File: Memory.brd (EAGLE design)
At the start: 105.4 x 56.8 mm, 4 parts, among them IC5 HM62256DIP

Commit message: Finish Modularization
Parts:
- removed IC5: HM62256DIP, jean:HM62256-DIP
- added IC1: AT28C256ZIF, bt_memory:DIL28-ZIF
- added IC2: HM62256DIP, jean:HM62256-DIP
- U$1: value AT28C256ZIF -> (none); device bt_memory:DIL28-ZIF -> bfl:OSHW2
- moved U$1 31.4 mm to (43.2, 7.62), turned to 0 degrees
- moved V2 20.7 mm to (96.5, 21.6)
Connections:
- net !RD: now also IC1.22, IC2.22; no longer IC5.22, U$1.22
- net !WR: now also IC1.27, IC2.27; no longer IC5.27, U$1.27
- net A0: now also IC1.10, IC2.10; no longer IC5.10, U$1.10
- net A1: now also IC1.9, IC2.9; no longer IC5.9, U$1.9
- net A10: now also IC1.21, IC2.21; no longer IC5.21, U$1.21
- net A11: now also IC1.23, IC2.23; no longer IC5.23, U$1.23
- net A12: now also IC1.2, IC2.2; no longer IC5.2, U$1.2
- net A13: now also IC1.26, IC2.26; no longer IC5.26, U$1.26
- net A14: now also IC1.1, IC2.1; no longer IC5.1, U$1.1
- net A2: now also IC1.8, IC2.8; no longer IC5.8, U$1.8
- net A3: now also IC1.7, IC2.7; no longer IC5.7, U$1.7
- net A4: now also IC1.6, IC2.6; no longer IC5.6, U$1.6
- net A5: now also IC1.5, IC2.5; no longer IC5.5, U$1.5
- net A6: now also IC1.4, IC2.4; no longer IC5.4, U$1.4
- net A7: now also IC1.3, IC2.3; no longer IC5.3, U$1.3
- net A8: now also IC1.25, IC2.25; no longer IC5.25, U$1.25
- net A9: now also IC1.24, IC2.24; no longer IC5.24, U$1.24
- net D0: now also IC1.11, IC2.11; no longer IC5.11, U$1.11
- net D1: now also IC1.12, IC2.12; no longer IC5.12, U$1.12
- net D2: now also IC1.13, IC2.13; no longer IC5.13, U$1.13
- net D3: now also IC1.15, IC2.15; no longer IC5.15, U$1.15
- net D4: now also IC1.16, IC2.16; no longer IC5.16, U$1.16
- net D5: now also IC1.17, IC2.17; no longer IC5.17, U$1.17
- net D6: now also IC1.18, IC2.18; no longer IC5.18, U$1.18
- net D7: now also IC1.19, IC2.19; no longer IC5.19, U$1.19
- net GND: now also IC1.14, IC2.14; no longer IC5.14, U$1.14
- net N$2: now also IC1.20; no longer U$1.20
- net N$9: now also IC2.20; no longer IC5.20
- net VCC: now also IC1.28, IC2.28; no longer IC5.28, U$1.28
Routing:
- net N$2: track 0.00 -> 150.9 mm, vias 0 -> 3
- net GND: track 0.00 -> 110.4 mm, vias 0 -> 1
- net !MREQ: track 13.3 -> 116.1 mm, vias 0 -> 2
- net VCC: track 27.7 -> 121.8 mm
- net A11: track 23.2 -> 98.3 mm, vias 0 -> 1
- net A15: track 11.2 -> 82.3 mm
- net D6: track 177.5 -> 109.8 mm, vias 0 -> 1
- net D4: track 200.1 -> 136.3 mm, vias 0 -> 2
- net A10: track 28.0 -> 91.5 mm, vias 0 -> 1
- net D5: track 191.5 -> 129.9 mm, vias 0 -> 4
- net !RD: track 44.8 -> 85.9 mm
- net !WR: track 68.9 -> 35.1 mm
- net A7: track 73.4 -> 41.1 mm
- net A6: track 75.3 -> 46.6 mm
- net D3: track 208.0 -> 179.5 mm, vias 0 -> 1
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- added copper zone on layer 1, net GND
- added copper zone on layer 16, net GND
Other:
- board size 105.4 x 56.8 mm -> 101.6 x 37.8 mm
- board text added: "CPD-80 Memory V1"

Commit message: Update names and font
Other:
- board text added: "CPD-80 Memory v1"
- board text removed: "CPD-80 Memory V1"
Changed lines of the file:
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@@
 <wire x1="102.85" y1="37.77" x2="1.27" y2="37.77" width="0.254" layer="20"/>
 <wire x1="1.27" y1="37.77" x2="1.27" y2="0" width="0.254" layer="20"/>
-<text x="2.54" y="33.02" size="1.778" layer="21">CPD-80 Memory V1</text>
+<text x="2.54" y="33.02" size="1.778" layer="21" font="fixed">CPD-80 Memory v1</text>
 <rectangle x1="98.7933" y1="31.8135" x2="99.1235" y2="31.8389" layer="21"/>
 <rectangle x1="98.5901" y1="31.8389" x2="99.1997" y2="31.8643" layer="21"/>

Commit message: Change Memoryboard
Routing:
- net VCC: track 121.8 -> 134.5 mm, vias 0 -> 1
- net !RD: track 85.9 -> 87.8 mm
- net !MREQ: track 116.1 -> 117.5 mm
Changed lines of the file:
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@@
 <setting verticaltext="up"/>
 </settings>
-<grid distance="0.05" unitdist="inch" unit="inch" style="lines" multiple="1" display="no" altdistance="0.005" altunitdist="inch" altunit="inch"/>
+<grid distance="0.05" unitdist="inch" unit="inch" style="lines" multiple="1" display="no" altdistance="0.025" altunitdist="inch" altunit="inch"/>
 <layers>
 <layer number="1" name="Top" color="4" fill="1" visible="yes" active="yes"/>
@@
 <contactref element="JP1" pad="5"/>
 <wire x1="13.716" y1="35.306" x2="7.62" y2="29.21" width="0.254" layer="1"/>
-<wire x1="88.9" y1="35.306" x2="76.454" y2="35.306" width="0.254" layer="1"/>
 <wire x1="76.454" y1="35.306" x2="13.716" y2="35.306" width="0.254" layer="1"/>
 <wire x1="96.52" y1="27.686" x2="88.9" y2="35.306" width="0.254" layer="1"/>
@@
 <wire x1="76.454" y1="35.306" x2="76.454" y2="34.036" width="0.254" layer="1"/>
 <via x="78.232" y="32.258" extent="1-16" drill="0.6096"/>
+<wire x1="76.454" y1="35.306" x2="88.9" y2="35.306" width="0.254" layer="1"/>
 </signal>
 <signal name="D3">
@@
 <wire x1="38.1" y1="8.89" x2="38.1" y2="13.97" width="0.254" layer="1"/>
 <wire x1="35.56" y1="6.35" x2="38.1" y2="8.89" width="0.254" layer="1"/>
-<wire x1="94.996" y1="29.21" x2="100.33" y2="29.21" width="0.254" layer="16"/>
-<wire x1="90.932" y1="33.274" x2="94.996" y2="29.21" width="0.254" layer="16"/>
-<wire x1="77.978" y1="33.274" x2="90.932" y2="33.274" width="0.254" layer="16"/>
-<wire x1="76.2" y1="31.496" x2="77.978" y2="33.274" width="0.254" layer="16"/>
-<wire x1="76.2" y1="26.416" x2="76.2" y2="31.496" width="0.254" layer="16"/>
-<wire x1="81.28" y1="21.336" x2="76.2" y2="26.416" width="0.254" layer="16"/>
-<wire x1="81.28" y1="12.954" x2="81.28" y2="21.336" width="0.254" layer="16"/>
-<wire x1="80.518" y1="12.192" x2="81.28" y2="12.954" width="0.254" layer="16"/>
-<wire x1="66.802" y1="12.192" x2="80.518" y2="12.192" width="0.254" layer="16"/>
-<wire x1="66.04" y1="12.954" x2="66.802" y2="12.192" width="0.254" layer="16"/>
-<wire x1="66.04" y1="18.034" x2="66.04" y2="12.954" width="0.254" layer="16"/>
-<wire x1="55.88" y1="28.194" x2="66.04" y2="18.034" width="0.254" layer="16"/>
-<wire x1="55.88" y1="30.226" x2="55.88" y2="28.194" width="0.254" layer="16"/>
-<wire x1="55.118" y1="30.988" x2="55.88" y2="30.226" width="0.254" layer="16"/>
-<wire x1="53.848" y1="30.988" x2="55.118" y2="30.988" width="0.254" layer="16"/>
-<wire x1="52.07" y1="29.21" x2="53.848" y2="30.988" width="0.254" layer="16"/>
-<wire x1="41.656" y1="13.97" x2="38.1" y2="13.97" width="0.254" layer="16"/>
-<wire x1="55.88" y1="28.194" x2="41.656" y2="13.97" width="0.254" layer="16"/>
+<wire x1="26.162" y1="12.446" x2="26.162" y2="10.922" width="0.254" layer="1"/>
+<wire x1="26.924" y1="13.208" x2="26.162" y2="12.446" width="0.254" layer="1"/>
+<wire x1="26.924" y1="15.24" x2="26.924" y2="13.208" width="0.254" layer="1"/>
+<wire x1="29.464" y1="17.78" x2="26.924" y2="15.24" width="0.254" layer="1"/>
+<wire x1="34.29" y1="17.78" x2="29.464" y2="17.78" width="0.254" layer="1"/>
+<wire x1="38.1" y1="13.97" x2="34.29" y2="17.78" width="0.254" layer="1"/>
+<wire x1="94.869" y1="29.2608" x2="100.1268" y2="29.2608" width="0.254" layer="16"/>
+<wire x1="90.9828" y1="33.147" x2="94.869" y2="29.2608" width="0.254" layer="16"/>
+<wire x1="77.724" y1="33.147" x2="90.9828" y2="33.147" width="0.254" layer="16"/>
+<wire x1="76.3524" y1="31.7754" x2="77.724" y2="33.147" width="0.254" layer="16"/>
+<wire x1="76.3524" y1="26.289" x2="76.3524" y2="31.7754" width="0.254" layer="16"/>
+<wire x1="81.153" y1="21.4884" x2="76.3524" y2="26.289" width="0.254" layer="16"/>
+<wire x1="81.153" y1="12.8016" x2="81.153" y2="21.4884" width="0.254" layer="16"/>
+<wire x1="80.4672" y1="12.1158" x2="81.153" y2="12.8016" width="0.254" layer="16"/>
+<wire x1="66.9798" y1="12.1158" x2="80.4672" y2="12.1158" width="0.254" layer="16"/>
+<wire x1="65.8368" y1="13.2588" x2="66.9798" y2="12.1158" width="0.254" layer="16"/>
+<wire x1="65.8368" y1="15.7734" x2="65.8368" y2="13.2588" width="0.254" layer="16"/>
+<wire x1="60.8076" y1="20.8026" x2="65.8368" y2="15.7734" width="0.254" layer="16"/>
+<wire x1="46.863" y1="20.8026" x2="53.4924" y2="20.8026" width="0.254" layer="16"/>
+<wire x1="53.4924" y1="20.8026" x2="60.8076" y2="20.8026" width="0.254" layer="16"/>
+<wire x1="40.2336" y1="14.1732" x2="46.863" y2="20.8026" width="0.254" layer="16"/>
+<wire x1="38.1762" y1="14.1732" x2="40.2336" y2="14.1732" width="0.254" layer="16"/>
+<wire x1="100.1268" y1="29.2608" x2="100.33" y2="29.21" width="0.254" layer="16"/>
+<wire x1="38.1762" y1="14.1732" x2="38.1" y2="13.97" width="0.254" layer="16"/>
+<wire x1="52.1208" y1="28.1178" x2="52.1208" y2="29.0322" width="0.254" layer="1"/>
+<wire x1="53.4924" y1="26.7462" x2="52.1208" y2="28.1178" width="0.254" layer="1"/>
+<wire x1="53.4924" y1="20.8026" x2="53.4924" y2="26.7462" width="0.254" layer="16"/>
+<wire x1="52.1208" y1="29.0322" x2="52.07" y2="29.21" width="0.254" layer="1"/>
+<via x="53.4924" y="26.7462" extent="1-16" drill="0.6096"/>
 </signal>
 <signal name="GND">
@@
 <wire x1="76.2" y1="12.954" x2="80.01" y2="9.144" width="0.254" layer="1"/>
 <wire x1="76.2" y1="30.226" x2="76.2" y2="12.954" width="0.254" layer="1"/>
-<wire x1="76.962" y1="30.988" x2="76.2" y2="30.226" width="0.254" layer="1"/>
-<wire x1="90.932" y1="30.988" x2="76.962" y2="30.988" width="0.254" layer="1"/>
-<wire x1="92.71" y1="29.21" x2="90.932" y2="30.988" width="0.254" layer="1"/>
 <via x="36.83" y="2.794" extent="1-16" drill="0.6096"/>
 <via x="62.23" y="2.794" extent="1-16" drill="0.6096"/>
+<wire x1="92.71" y1="29.21" x2="92.71" y2="30.48" width="0.254" layer="1"/>
+<wire x1="92.71" y1="30.48" x2="91.44" y2="31.75" width="0.254" layer="1"/>
+<wire x1="91.44" y1="31.75" x2="82.55" y2="31.75" width="0.254" layer="1"/>
+<wire x1="82.55" y1="31.75" x2="81.915" y2="31.115" width="0.254" layer="1"/>
+<wire x1="81.915" y1="31.115" x2="77.089" y2="31.115" width="0.254" layer="1"/>
+<wire x1="77.089" y1="31.115" x2="76.2" y2="30.226" width="0.254" layer="1"/>
 </signal>
 <signal name="N$9">
@@
 <contactref element="IC1" pad="22"/>
 <contactref element="JP1" pad="55"/>
-<wire x1="28.702" y1="8.128" x2="22.86" y2="13.97" width="0.254" layer="16"/>
-<wire x1="31.242" y1="8.128" x2="28.702" y2="8.128" width="0.254" layer="16"/>
+<wire x1="31.242" y1="8.128" x2="29.21" y2="8.128" width="0.254" layer="16"/>
+<wire x1="29.21" y1="8.128" x2="28.702" y2="8.128" width="0.254" layer="16"/>
 <wire x1="33.02" y1="6.35" x2="31.242" y2="8.128" width="0.254" layer="16"/>
 <wire x1="62.992" y1="33.528" x2="67.31" y2="29.21" width="0.254" layer="1"/>
@@
 <wire x1="16.764" y1="20.066" x2="16.764" y2="30.48" width="0.254" layer="1"/>
 <wire x1="22.86" y1="13.97" x2="16.764" y2="20.066" width="0.254" layer="1"/>
+<wire x1="29.21" y1="8.89" x2="29.21" y2="8.128" width="0.254" layer="16"/>
+<wire x1="27.686" y1="10.414" x2="29.21" y2="8.89" width="0.254" layer="16"/>
+<wire x1="27.686" y1="10.668" x2="27.686" y2="10.414" width="0.254" layer="16"/>
+<wire x1="26.416" y1="11.938" x2="27.686" y2="10.668" width="0.254" layer="16"/>
+<wire x1="25.654" y1="11.938" x2="26.416" y2="11.938" width="0.254" layer="16"/>
+<wire x1="25.146" y1="11.43" x2="25.654" y2="11.938" width="0.254" layer="16"/>
+<wire x1="24.892" y1="11.43" x2="25.146" y2="11.43" width="0.254" layer="16"/>
+<wire x1="22.86" y1="13.462" x2="24.892" y2="11.43" width="0.254" layer="16"/>
+<wire x1="22.86" y1="13.97" x2="22.86" y2="13.462" width="0.254" layer="16"/>
 </signal>
 <signal name="N$2">

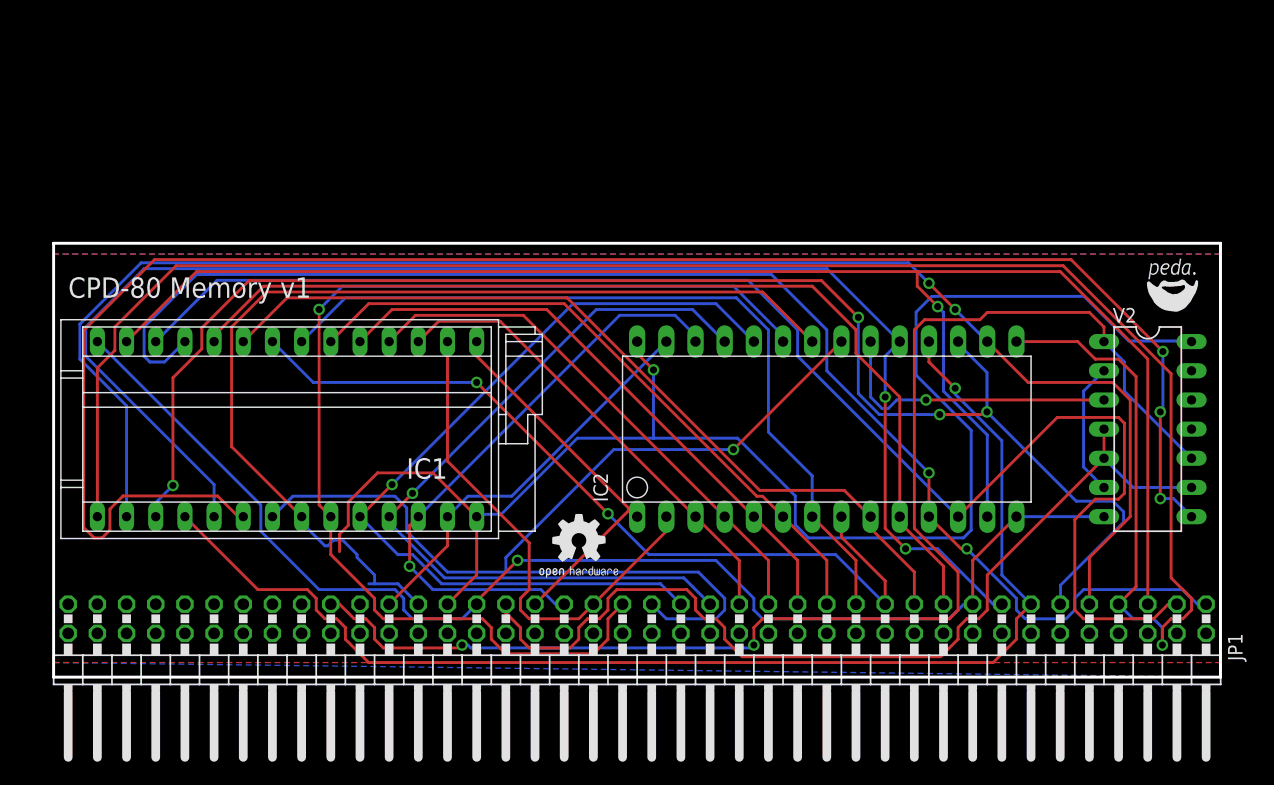
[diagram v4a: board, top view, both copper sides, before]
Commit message: Add Decoupling Capacitors.
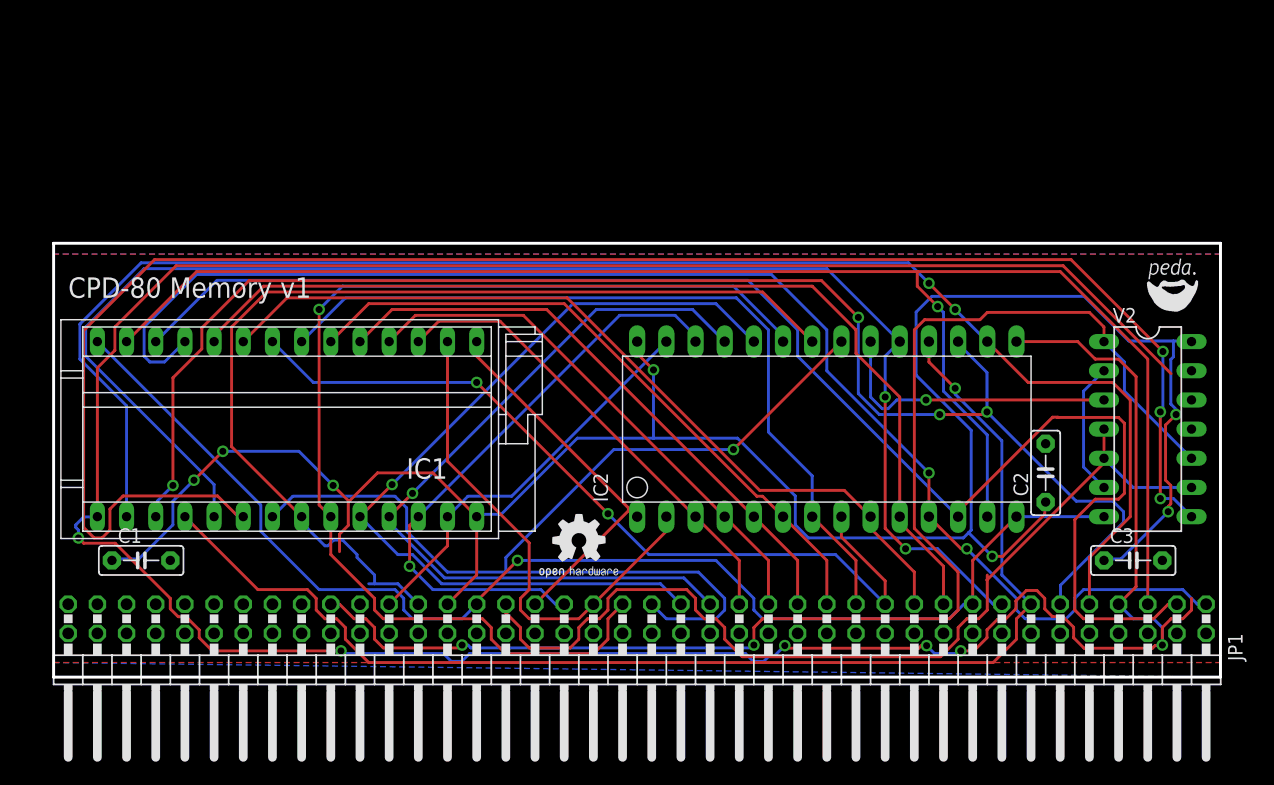
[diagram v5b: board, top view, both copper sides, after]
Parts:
- added C1, C2, C3: 0.1µF, capacitor-wima:C5B2.5
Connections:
- net GND: now also C1.2, C2.2, C3.2
- net VCC: now also C1.1, C2.1, C3.1
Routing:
- net D3: track 179.5 -> 270.3 mm, vias 1 -> 6
- net VCC: track 134.5 -> 195.4 mm, vias 1 -> 7

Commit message: Add Ground Rail to JEANNECTOR
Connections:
- net GND: now also JP1.10, JP1.12, JP1.14, JP1.16, JP1.18, JP1.2, JP1.20, JP1.22, JP1.24, JP1.26, JP1.28, JP1.30, JP1.32, JP1.34, JP1.36, JP1.38, JP1.4, JP1.40, JP1.42, JP1.44, JP1.46, JP1.48, JP1.50, JP1.52, JP1.54, JP1.56, JP1.58, JP1.6, JP1.60, JP1.62, JP1.64, JP1.66, JP1.68, JP1.70, JP1.72, JP1.74, JP1.76, JP1.78, JP1.8, JP1.80
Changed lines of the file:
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@@
 <contactref element="C2" pad="2"/>
 <contactref element="C3" pad="2"/>
-<wire x1="92.71" y1="13.97" x2="97.79" y2="10.16" width="0" layer="19" extent="1-1"/>
+<contactref element="JP1" pad="2"/>
+<contactref element="JP1" pad="4"/>
+<contactref element="JP1" pad="6"/>
+<contactref element="JP1" pad="8"/>
+<contactref element="JP1" pad="10"/>
+<contactref element="JP1" pad="12"/>
+<contactref element="JP1" pad="14"/>
+<contactref element="JP1" pad="16"/>
+<contactref element="JP1" pad="18"/>
+<contactref element="JP1" pad="20"/>
+<contactref element="JP1" pad="22"/>
+<contactref element="JP1" pad="24"/>
+<contactref element="JP1" pad="26"/>
+<contactref element="JP1" pad="28"/>
+<contactref element="JP1" pad="30"/>
+<contactref element="JP1" pad="32"/>
+<contactref element="JP1" pad="34"/>
+<contactref element="JP1" pad="36"/>
+<contactref element="JP1" pad="38"/>
+<contactref element="JP1" pad="40"/>
+<contactref element="JP1" pad="42"/>
+<contactref element="JP1" pad="44"/>
+<contactref element="JP1" pad="46"/>
+<contactref element="JP1" pad="48"/>
+<contactref element="JP1" pad="50"/>
+<contactref element="JP1" pad="52"/>
+<contactref element="JP1" pad="54"/>
+<contactref element="JP1" pad="56"/>
+<contactref element="JP1" pad="58"/>
+<contactref element="JP1" pad="60"/>
+<contactref element="JP1" pad="62"/>
+<contactref element="JP1" pad="64"/>
+<contactref element="JP1" pad="66"/>
+<contactref element="JP1" pad="68"/>
+<contactref element="JP1" pad="70"/>
+<contactref element="JP1" pad="72"/>
+<contactref element="JP1" pad="74"/>
+<contactref element="JP1" pad="76"/>
+<contactref element="JP1" pad="78"/>
+<contactref element="JP1" pad="80"/>
+<wire x1="97.79" y1="10.16" x2="92.71" y2="13.97" width="0" layer="19" extent="1-1"/>
 </signal>
 <signal name="!MREQ">

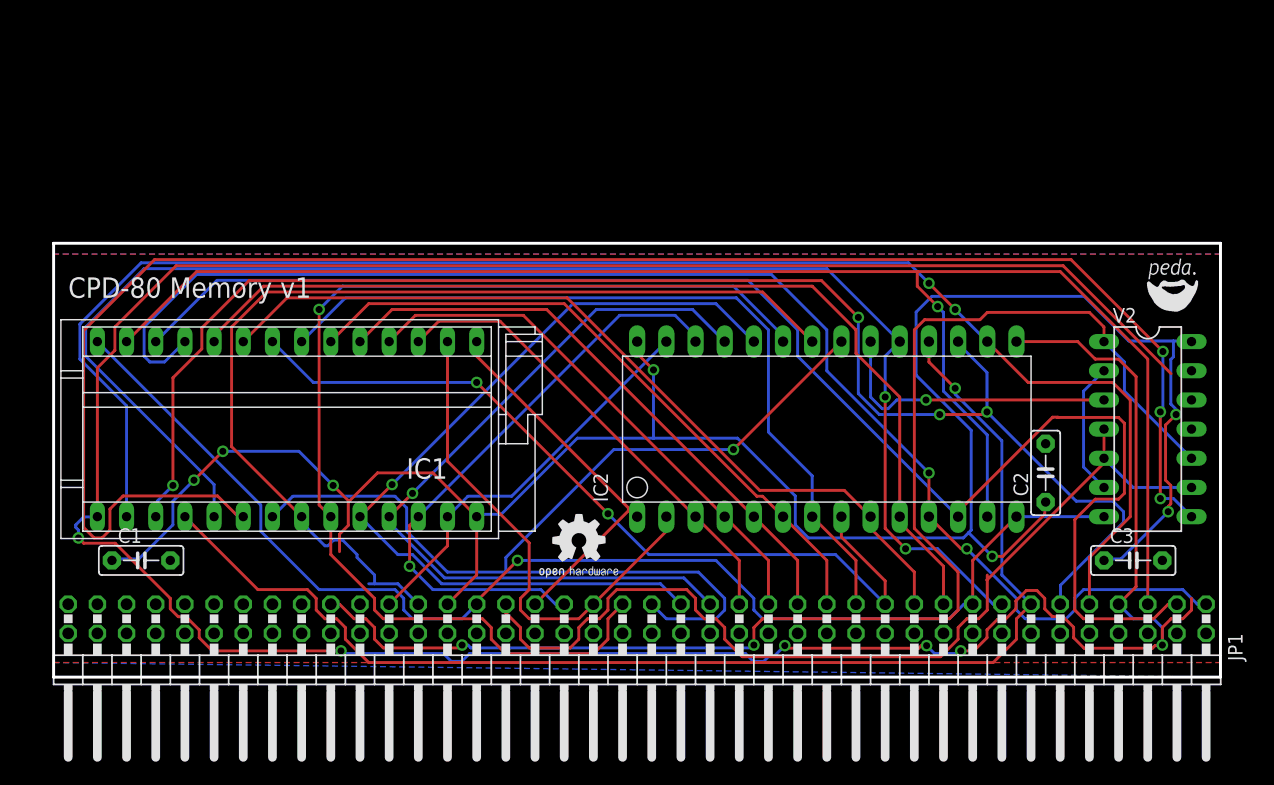
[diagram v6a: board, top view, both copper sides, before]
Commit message: Make Top Plane a VCC Plane instead of Ground, add Holes
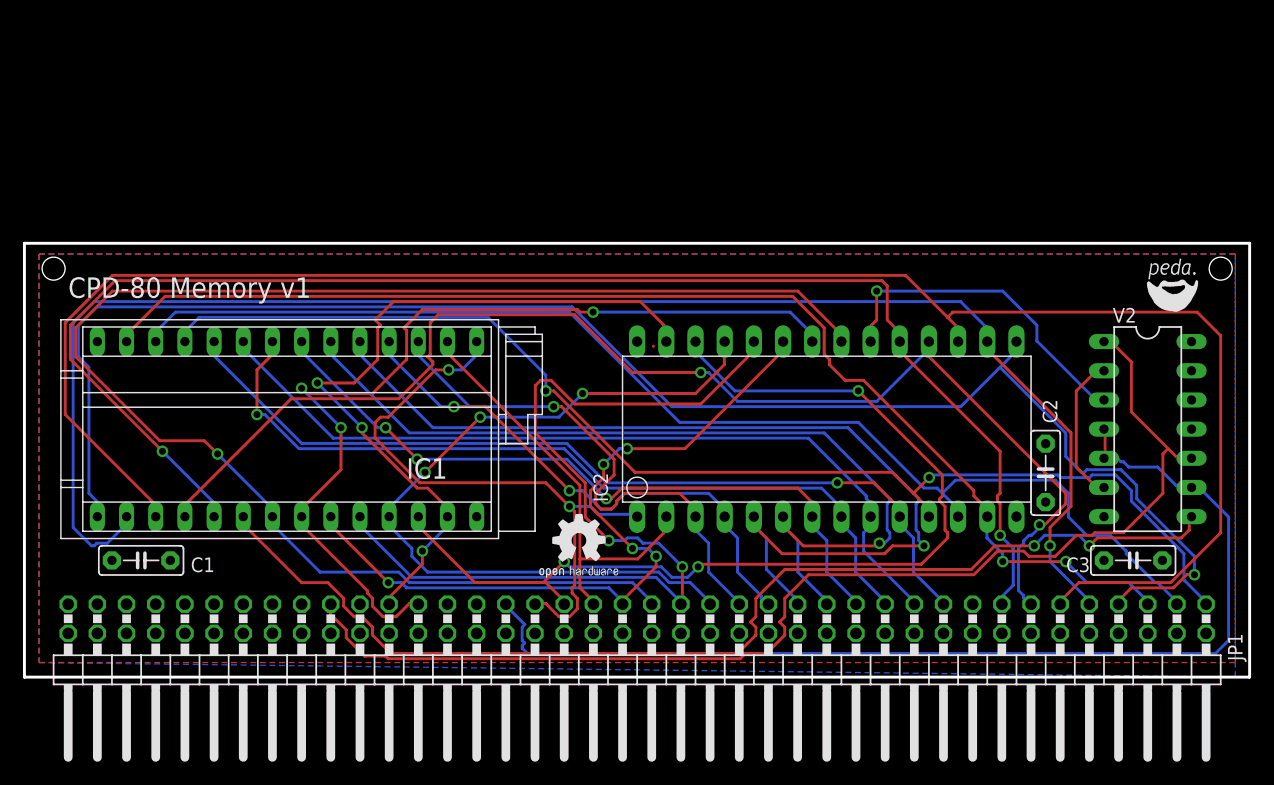
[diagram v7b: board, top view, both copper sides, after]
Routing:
- net VCC: track 195.4 -> 0.03 mm, vias 7 -> 0
- net D3: track 270.3 -> 141.4 mm, vias 6 -> 1
- net GND: track 110.4 -> 0.00 mm, vias 1 -> 0
- net N$2: track 150.9 -> 97.3 mm, vias 3 -> 2
- net A10: track 91.5 -> 132.9 mm
- net A13: track 52.1 -> 87.2 mm, vias 1 -> 3
- net D2: track 139.8 -> 105.9 mm, vias 1 -> 2
- net A5: track 52.1 -> 85.8 mm, vias 0 -> 1
- net D5: track 129.9 -> 161.3 mm, vias 4 -> 0
- net A11: track 98.3 -> 67.0 mm, vias 1 -> 5
- net !WR: track 35.1 -> 64.7 mm, vias 0 -> 3
- net D1: track 129.5 -> 106.0 mm
- net A4: track 57.6 -> 79.0 mm, vias 0 -> 1
- net A14: track 32.8 -> 53.3 mm, vias 0 -> 2
- net !MREQ: track 117.5 -> 102.4 mm, vias 2 -> 0
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- added copper zone on layer 1, net VCC
- removed copper zone on layer 1, net GND
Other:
- board size 101.6 x 37.8 mm -> 106.7 x 37.8 mm
